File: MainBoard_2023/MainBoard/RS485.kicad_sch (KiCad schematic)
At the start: 31 parts, among them J10 Conn_01x04, J11 Conn_01x04, J12 Conn_01x04, J13 Conn_01x04, J8 Conn_01x04, J9 Conn_01x04, U10 MAX3485, U11 LTC1480CN8#PBF, U12 MAX3485, U13 LTC1480CN8#PBF, U7 MAX3485, U8 TC7S14F, U9 LTC1480CN8#PBF

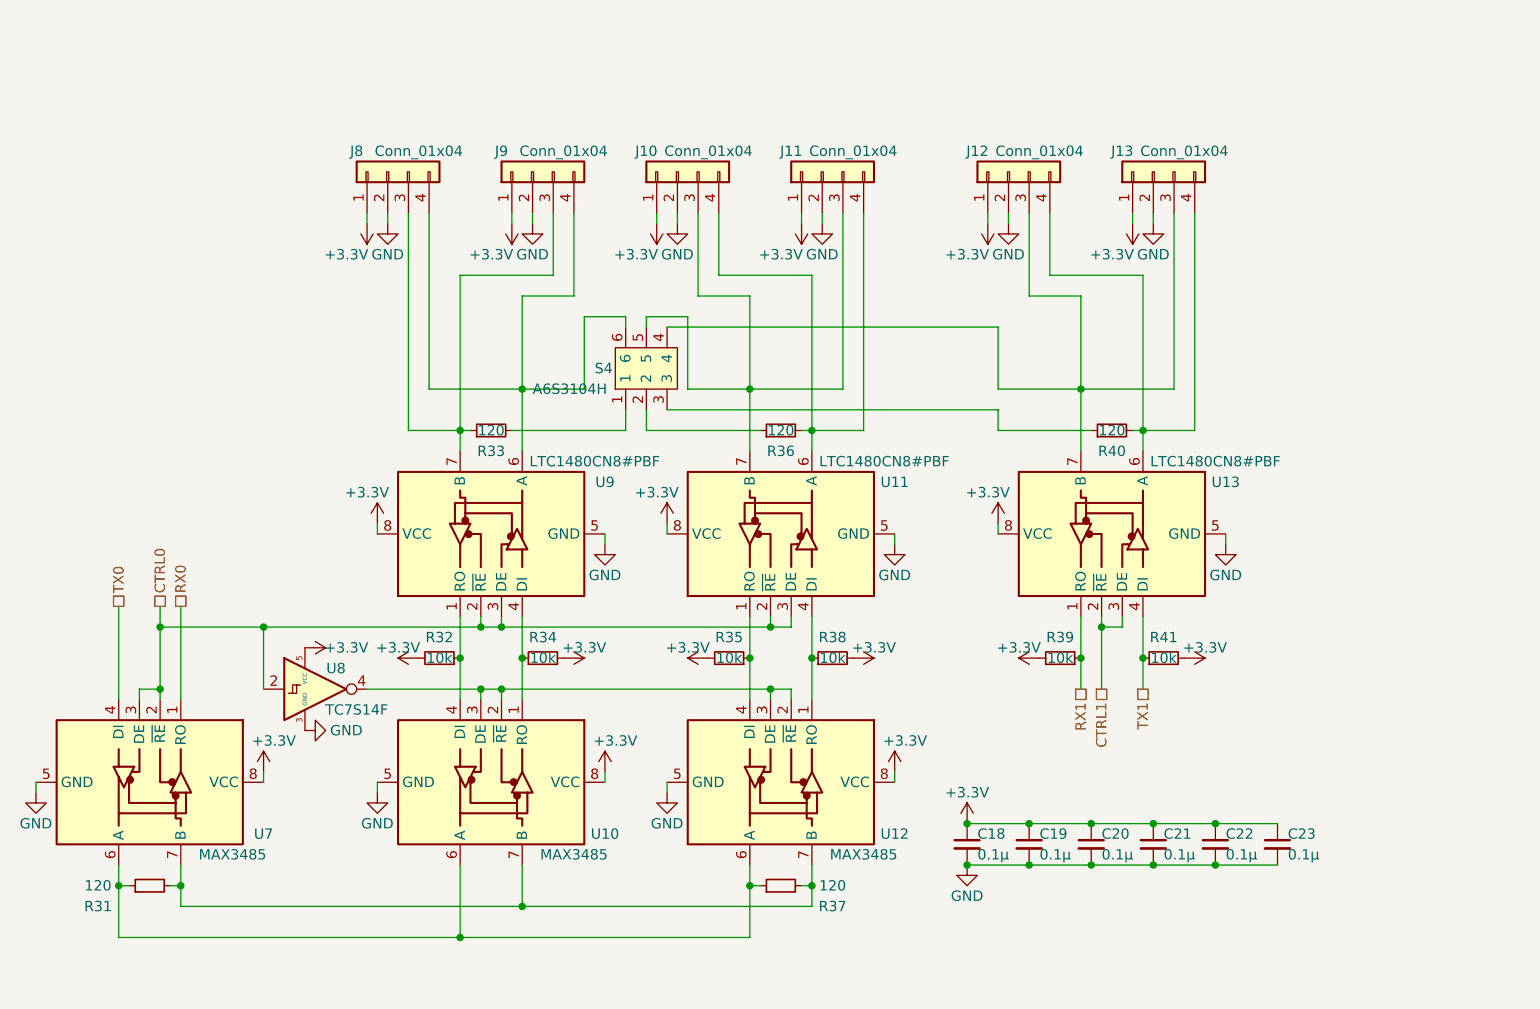
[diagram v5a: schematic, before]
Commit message: 回路図とPCBを変更
RJコネクタに変更
秋月のBNO055に変更
気圧センサのフットプリントを変更
ブロックタイプエミフィルのパッドを縮小
外形と取り付け穴を設定
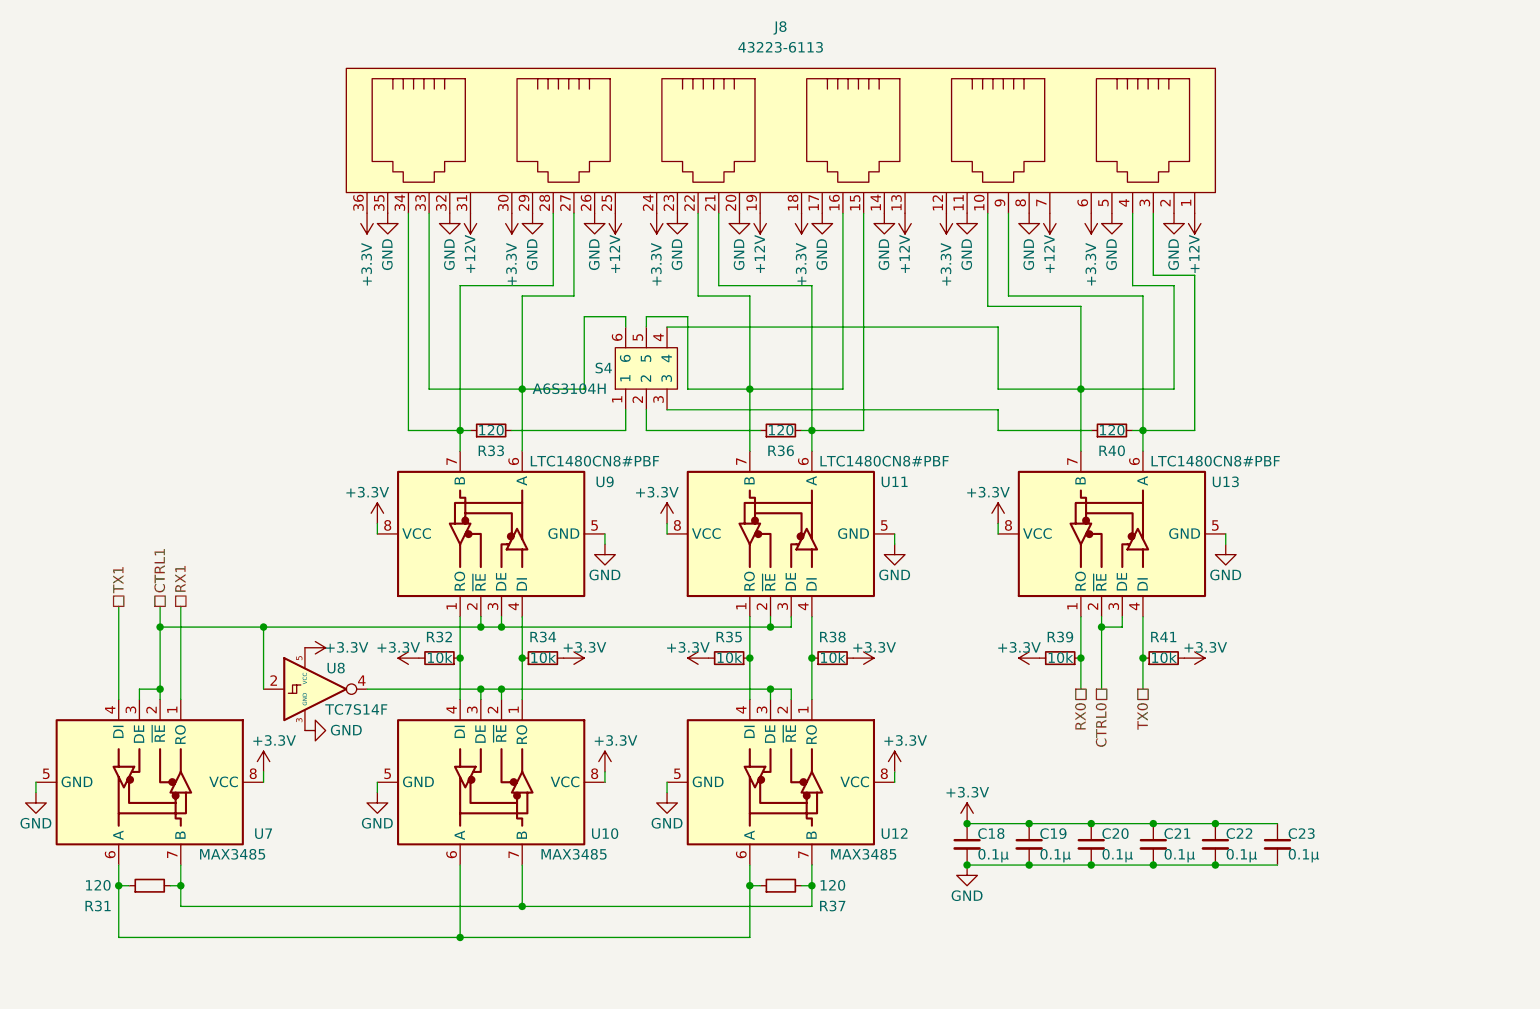
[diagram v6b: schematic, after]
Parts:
- removed J10, J11, J12, J13, J8, J9: Conn_01x04, Connector_JST:JST_XA_S04B-XASK-1_1x04_P2.50mm_Horizontal, symbol Connector_Generic:Conn_01x04
- added J8: 43223-6113, Molex_6P6C_Right_Angle_TH_RJ11_Modular_Jack_Connector_6Ports:Molex_6P6C_Right_Angle_TH_RJ11_Modular_Jack_Connector, symbol Molex_6P6C_Right_Angle_TH_RJ11_Modular_Jack_Connector_6Ports:43223-6113
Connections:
- net +3.3V: now also J8.12, J8.18, J8.24, J8.30, J8.36, J8.6
- net CTRL0: now also U13.2 (~{RE}), U13.3 (DE); no longer U11.2 (~{RE}), U11.3 (DE), U7.2 (~{RE}), U7.3 (DE), U8.2, U9.2 (~{RE}), U9.3 (DE)
- net CTRL1: now also U11.2 (~{RE}), U11.3 (DE), U7.2 (~{RE}), U7.3 (DE), U8.2, U9.2 (~{RE}), U9.3 (DE); no longer U13.2 (~{RE}), U13.3 (DE)
- net GND: now also J8.11, J8.14, J8.17, J8.2, J8.20, J8.23, J8.26, J8.29, J8.32, J8.35, J8.5, J8.8
- net RX0: now also R39.1, U13.1 (RO); no longer U7.1 (RO)
- net RX1: now also U7.1 (RO); no longer R39.1, U13.1 (RO)
- net TX0: now also R41.1, U13.4 (DI); no longer U7.4 (DI)
- net TX1: now also U7.4 (DI); no longer R41.1, U13.4 (DI)
- net at S4.5, U11.7 (B): now also J8.16, J8.22
- net at R36.2, U11.6 (A): now also J8.15, J8.21
- net at R33.1, U9.7 (B): now also J8.28, J8.34
- net at R40.2, U13.6 (A): now also J8.3, J8.9
- net at S4.4, U13.7 (B): now also J8.10, J8.4
- net at S4.6, U9.6 (A): now also J8.27, J8.33
- new net +12V: J8.1, J8.13, J8.19, J8.25, J8.31, J8.7

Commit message: シルクを整えた
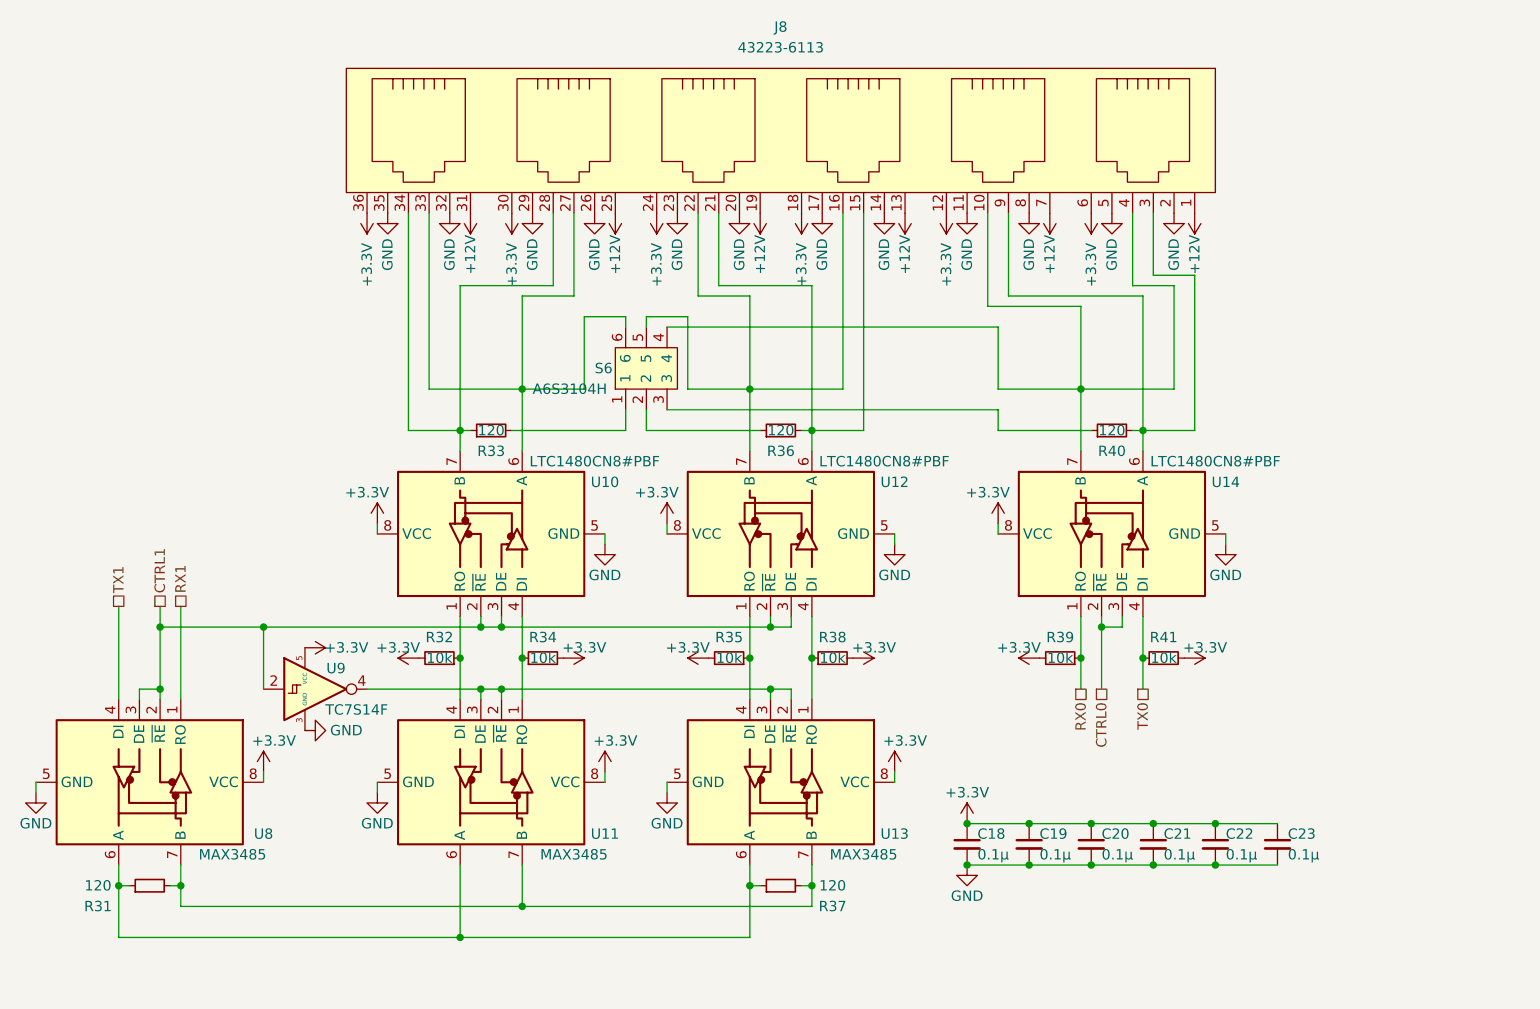
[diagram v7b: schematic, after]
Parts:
- renumbered S4 to S6, U9 to U10, U10 to U11, U11 to U12, U12 to U13, U13 to U14, U7 to U8, U8 to U9
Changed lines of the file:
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@@
   (symbol (lib_id "Interface_UART:MAX485E") (at 194.31 96.52 90) (unit 1)
     (in_bom yes) (on_board yes)
-    (property "Reference" "U13" (id 0) (at 209.55 90.17 90))
+    (property "Reference" "U14" (id 0) (at 209.55 90.17 90))
     (property "Value" "LTC1480CN8#PBF" (id 1) (at 208.28 87.63 90))
     (property "Footprint" "Package_DIP:DIP-8_W7.62mm_LongPads" (id 2) (at 212.09 96.52 0)
@@
   (symbol (lib_id "Interface_UART:MAX485E") (at 153.67 96.52 90) (unit 1)
     (in_bom yes) (on_board yes)
-    (property "Reference" "U11" (id 0) (at 168.91 90.17 90))
+    (property "Reference" "U12" (id 0) (at 168.91 90.17 90))
     (property "Value" "LTC1480CN8#PBF" (id 1) (at 167.64 87.63 90))
     (property "Footprint" "Package_DIP:DIP-8_W7.62mm_LongPads" (id 2) (at 171.45 96.52 0)
@@
   (symbol (lib_id "Interface_UART:MAX3485") (at 156.21 127 270) (unit 1)
     (in_bom yes) (on_board yes)
-    (property "Reference" "U12" (id 0) (at 168.91 133.35 90))
+    (property "Reference" "U13" (id 0) (at 168.91 133.35 90))
     (property "Value" "MAX3485" (id 1) (at 165.1 135.89 90))
     (property "Footprint" "MAX3485ECSA:MAX3485ECSA" (id 2) (at 138.43 127 0)
@@
   (symbol (lib_id "Interface_UART:MAX3485") (at 120.65 127 270) (unit 1)
     (in_bom yes) (on_board yes)
-    (property "Reference" "U10" (id 0) (at 133.35 133.35 90))
+    (property "Reference" "U11" (id 0) (at 133.35 133.35 90))
     (property "Value" "MAX3485" (id 1) (at 129.54 135.89 90))
     (property "Footprint" "MAX3485ECSA:MAX3485ECSA" (id 2) (at 102.87 127 0)
@@
   (symbol (lib_id "Interface_UART:MAX485E") (at 118.11 96.52 90) (unit 1)
     (in_bom yes) (on_board yes)
-    (property "Reference" "U9" (id 0) (at 133.35 90.17 90))
+    (property "Reference" "U10" (id 0) (at 133.35 90.17 90))
     (property "Value" "LTC1480CN8#PBF" (id 1) (at 132.08 87.63 90))
     (property "Footprint" "Package_DIP:DIP-8_W7.62mm_LongPads" (id 2) (at 135.89 96.52 0)
@@
   (symbol (lib_id "Interface_UART:MAX3485") (at 78.74 127 270) (unit 1)
     (in_bom yes) (on_board yes)
-    (property "Reference" "U7" (id 0) (at 91.44 133.35 90))
+    (property "Reference" "U8" (id 0) (at 91.44 133.35 90))
     (property "Value" "MAX3485" (id 1) (at 87.63 135.89 90))
     (property "Footprint" "MAX3485ECSA:MAX3485ECSA" (id 2) (at 60.96 127 0)
@@
   (symbol (lib_id "74xGxx:SN74LVC1G14DBV") (at 96.52 115.57 0) (unit 1)
     (in_bom yes) (on_board yes)
-    (property "Reference" "U8" (id 0) (at 100.33 113.03 0))
+    (property "Reference" "U9" (id 0) (at 100.33 113.03 0))
     (property "Value" "TC7S14F" (id 1) (at 102.87 118.11 0))
     (property "Footprint" "TC7S14F:TC7S14F" (id 2) (at 96.52 121.92 0)
@@
   (symbol (lib_id "A6S-3104-H:A6S3104H") (at 135.89 81.28 90) (unit 1)
     (in_bom yes) (on_board yes)
-    (property "Reference" "S4" (id 0) (at 132.08 76.2 90)
+    (property "Reference" "S6" (id 0) (at 132.08 76.2 90)
       (effects (font (size 1.27 1.27)) (justify right))
     )
